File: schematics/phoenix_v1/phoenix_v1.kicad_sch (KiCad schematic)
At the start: 18 parts, among them J1 Screw_Terminal_01x02, J2 Conn_01x09_Socket, SW1 RotaryEncoder_Switch, U1 ESP32-S3-DevKitC, U2 NHD-C0220BIZ

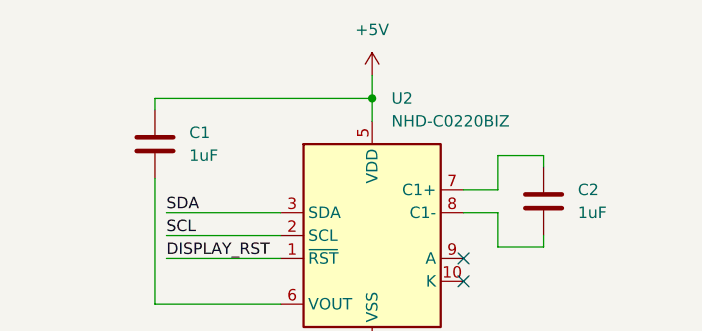
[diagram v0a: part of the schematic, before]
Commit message: fix "NHD-CO22BIZ needs 3.3V not 5V"
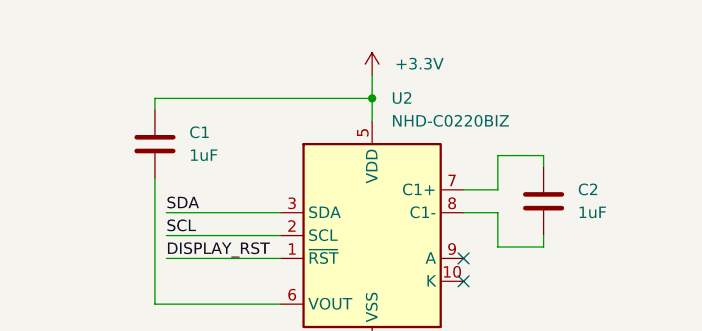
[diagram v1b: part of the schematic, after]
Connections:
- net +3.3V: now also C1.1, U2.5 (VDD)
- net +5V: no longer C1.1, U2.5 (VDD)
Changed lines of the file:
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@@
 			)
 		)
-		(property "Value" "+5V"
-			(at 168.91 19.05 0)
+		(property "Value" "+3.3V"
+			(at 171.45 22.8599 0)
 			(effects
 				(font
 					(size 1.27 1.27)
 				)
+				(justify left)
 			)
 		)

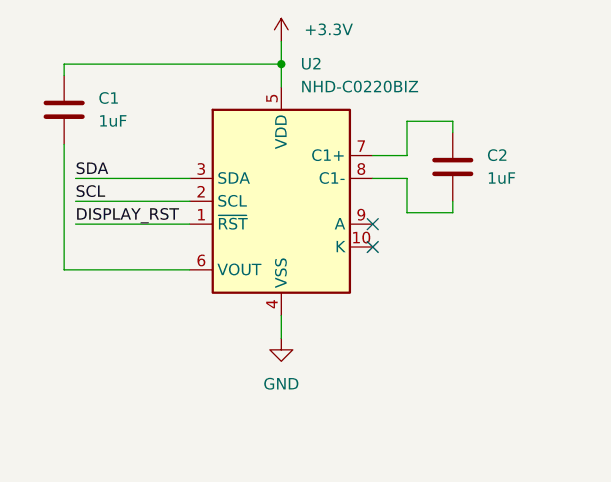
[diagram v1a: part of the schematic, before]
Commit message: connect A and K on lcd
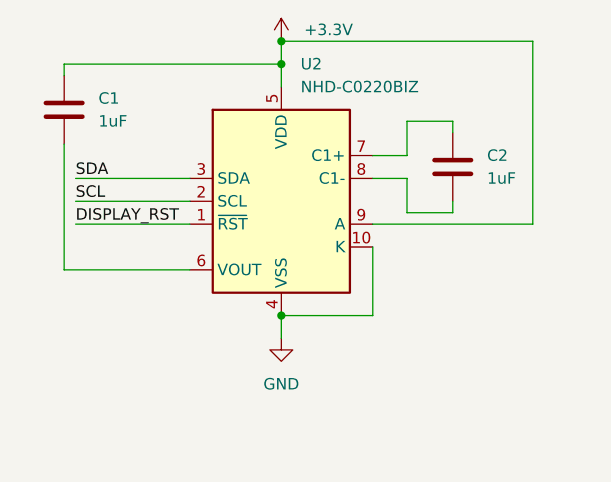
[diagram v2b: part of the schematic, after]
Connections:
- net +3.3V: now also U2.9 (A)
- net GND: now also U2.10 (K)
- no-connect marks 3 -> 1
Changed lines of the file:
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@@
+	)
+	(junction
+		(at 168.91 24.13)
+		(diameter 0)
+		(color 0 0 0 0)
 	)
 	(junction
@@
 	)
 	(junction
+		(at 168.91 54.61)
+		(diameter 0)
+		(color 0 0 0 0)
+	)
+	(junction
 		(at 43.18 41.91)
 		(diameter 0)
@@
 		(at 114.3 175.26)
 	)
-	(no_connect
-		(at 179.07 44.45)
-	)
-	(no_connect
-		(at 179.07 46.99)
-	)
 	(wire
 		(pts
@@
 	(wire
 		(pts
+			(xy 179.07 44.45) (xy 196.85 44.45)
+		)
+		(stroke
+			(width 0)
+			(type default)
+		)
+	)
+	(wire
+		(pts
 			(xy 46.99 96.52) (xy 50.8 96.52)
 		)
@@
 	(wire
 		(pts
+			(xy 196.85 44.45) (xy 196.85 24.13)
+		)
+		(stroke
+			(width 0)
+			(type default)
+		)
+	)
+	(wire
+		(pts
+			(xy 179.07 46.99) (xy 179.07 54.61)
+		)
+		(stroke
+			(width 0)
+			(type default)
+		)
+	)
+	(wire
+		(pts
 			(xy 132.08 88.9) (xy 119.38 88.9)
 		)
@@
 	(wire
 		(pts
+			(xy 179.07 54.61) (xy 168.91 54.61)
+		)
+		(stroke
+			(width 0)
+			(type default)
+		)
+	)
+	(wire
+		(pts
 			(xy 119.38 99.06) (xy 142.24 99.06)
 		)
@@
 		)
 		(stroke
+			(width 0)
+			(type default)
+		)
+	)
+	(wire
+		(pts
+			(xy 168.91 24.13) (xy 196.85 24.13)
+		)
+		(stroke
